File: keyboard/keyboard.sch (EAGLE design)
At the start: 39 parts, among them SW1 CHERRY_MX, SW10 CHERRY_MX, SW11 CHERRY_MX, SW12 CHERRY_MX, SW13 CHERRY_MX, SW14 CHERRY_MX, SW15 CHERRY_MX, SW16 CHERRY_MX, SW17 CHERRY_MX, SW18 CHERRY_MX, SW19 CHERRY_MX, SW2 CHERRY_MX, SW20 CHERRY_MX, SW21 CHERRY_MX, SW22 CHERRY_MX, SW23 CHERRY_MX, SW24 CHERRY_MX, SW25 CHERRY_MX, SW26 CHERRY_MX, SW27 CHERRY_MX, SW28 CHERRY_MX, SW3 CHERRY_MX, SW4 CHERRY_MX, SW5 CHERRY_MX, SW6 CHERRY_MX, SW7 CHERRY_MX, SW8 CHERRY_MX, SW9 CHERRY_MX

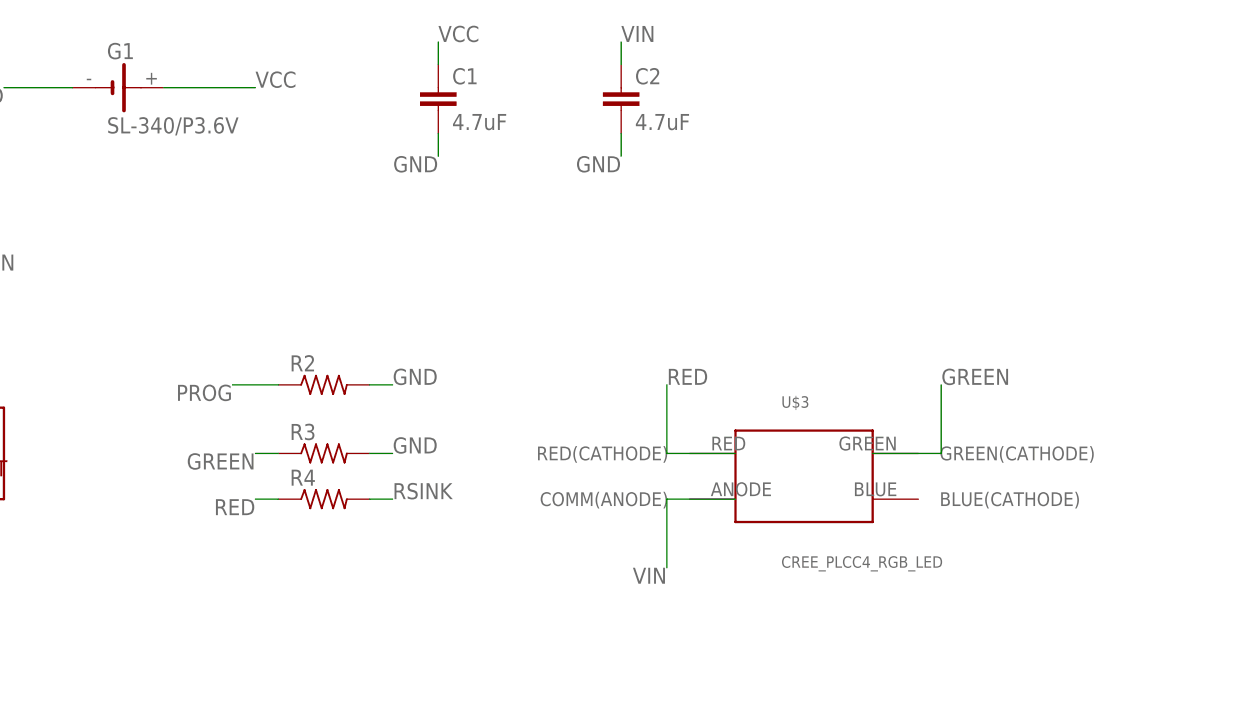
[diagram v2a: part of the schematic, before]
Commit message: add GRM32ER71H475KA88L capacitor
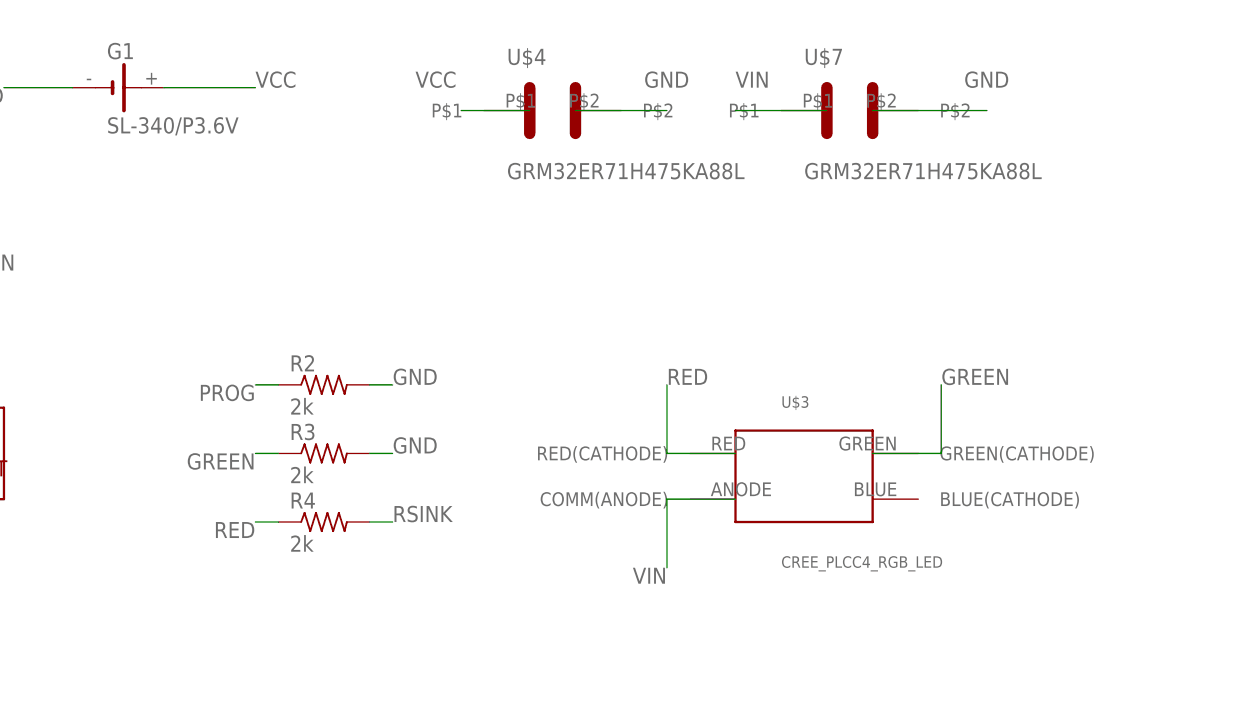
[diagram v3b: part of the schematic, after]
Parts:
- removed C1, C2: 4.7uF, capacitor-wima:C2.5/5
- added U$4, U$7: GRM32ER71H475KA88L, GRM32ER71H475KA88L:GRM32ER71H475KA88L
- R2, R3, R4: value (none) -> 2k
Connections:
- net GND: now also U$4.P$2, U$7.P$2; no longer C1.2, C2.2
- net VCC: now also U$4.P$1; no longer C1.1
- net VIN: now also U$7.P$1; no longer C2.1
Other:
- moved on the sheet: R4
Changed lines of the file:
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@@
 <part name="U$2" library="mcp73831t" deviceset="MCP73831T" device=""/>
 <part name="G1" library="battery" library_urn="urn:adsk.eagle:library:109" deviceset="SL-340/P3.6V" device="" package3d_urn="urn:adsk.eagle:package:4605/1"/>
-<part name="C1" library="capacitor-wima" library_urn="urn:adsk.eagle:library:116" deviceset="C" device="2.5/5" package3d_urn="urn:adsk.eagle:package:5407/1" value="4.7uF"/>
-<part name="C2" library="capacitor-wima" library_urn="urn:adsk.eagle:library:116" deviceset="C" device="2.5/5" package3d_urn="urn:adsk.eagle:package:5407/1" value="4.7uF"/>
 <part name="U$6" library="core51822b" deviceset="CORE51822B" device=""/>
-<part name="R2" library="resistor" library_urn="urn:adsk.eagle:library:348" deviceset="R-US_" device="R1210" package3d_urn="urn:adsk.eagle:package:26063/1"/>
-<part name="R3" library="resistor" library_urn="urn:adsk.eagle:library:348" deviceset="R-US_" device="R1210" package3d_urn="urn:adsk.eagle:package:26063/1"/>
-<part name="R4" library="resistor" library_urn="urn:adsk.eagle:library:348" deviceset="R-US_" device="R1210" package3d_urn="urn:adsk.eagle:package:26063/1"/>
+<part name="R2" library="resistor" library_urn="urn:adsk.eagle:library:348" deviceset="R-US_" device="R1210" package3d_urn="urn:adsk.eagle:package:26063/1" value="2k"/>
+<part name="R3" library="resistor" library_urn="urn:adsk.eagle:library:348" deviceset="R-US_" device="R1210" package3d_urn="urn:adsk.eagle:package:26063/1" value="2k"/>
+<part name="R4" library="resistor" library_urn="urn:adsk.eagle:library:348" deviceset="R-US_" device="R1210" package3d_urn="urn:adsk.eagle:package:26063/1" value="2k"/>
+<part name="U$4" library="GRM32ER71H475KA88L" deviceset="GRM32ER71H475KA88L" device=""/>
+<part name="U$7" library="GRM32ER71H475KA88L" deviceset="GRM32ER71H475KA88L" device=""/>
 </parts>
 <sheets>
@@
 <instance part="U$2" gate="G$1" x="45.72" y="33.02"/>
 <instance part="G1" gate="G$1" x="66.04" y="73.66"/>
-<instance part="C1" gate="G$1" x="101.6" y="73.66"/>
-<instance part="C2" gate="G$1" x="121.92" y="73.66"/>
 <instance part="U$6" gate="G$1" x="256.54" y="-264.16"/>
 <instance part="R2" gate="G$1" x="88.9" y="40.64"/>
 <instance part="R3" gate="G$1" x="88.9" y="33.02"/>
-<instance part="R4" gate="G$1" x="88.9" y="27.94"/>
+<instance part="R4" gate="G$1" x="88.9" y="25.4"/>
+<instance part="U$4" gate="G$1" x="114.3" y="71.12"/>
+<instance part="U$7" gate="G$1" x="147.32" y="71.12"/>
 </instances>
 <busses>
@@
 </segment>
 <segment>
-<pinref part="C1" gate="G$1" pin="2"/>
-<wire x1="101.6" y1="68.58" x2="101.6" y2="66.04" width="0.1524" layer="91"/>
-<label x="101.6" y="66.04" size="1.778" layer="95" rot="R180"/>
-</segment>
-<segment>
-<pinref part="C2" gate="G$1" pin="2"/>
-<wire x1="121.92" y1="68.58" x2="121.92" y2="66.04" width="0.1524" layer="91"/>
-<label x="121.92" y="66.04" size="1.778" layer="95" rot="R180"/>
-</segment>
-<segment>
 <pinref part="U$6" gate="G$1" pin="GND0"/>
 <wire x1="236.22" y1="-248.92" x2="218.44" y2="-248.92" width="0.1524" layer="91"/>
@@
 <wire x1="93.98" y1="40.64" x2="96.52" y2="40.64" width="0.1524" layer="91"/>
 <label x="96.52" y="40.64" size="1.778" layer="95"/>
+</segment>
+<segment>
+<pinref part="U$4" gate="G$1" pin="P$2"/>
+<wire x1="116.84" y1="71.12" x2="127" y2="71.12" width="0.1524" layer="91"/>
+<label x="124.46" y="73.66" size="1.778" layer="95"/>
+</segment>
+<segment>
+<pinref part="U$7" gate="G$1" pin="P$2"/>
+<wire x1="149.86" y1="71.12" x2="162.56" y2="71.12" width="0.1524" layer="91"/>
+<label x="160.02" y="73.66" size="1.778" layer="95"/>
 </segment>
 </net>
@@
 </segment>
 <segment>
-<pinref part="C1" gate="G$1" pin="1"/>
-<wire x1="101.6" y1="76.2" x2="101.6" y2="78.74" width="0.1524" layer="91"/>
-<label x="101.6" y="78.74" size="1.778" layer="95"/>
-</segment>
-<segment>
 <pinref part="U$6" gate="G$1" pin="VCC"/>
 <wire x1="236.22" y1="-276.86" x2="218.44" y2="-276.86" width="0.1524" layer="91"/>
 <label x="208.28" y="-276.86" size="1.778" layer="95"/>
+</segment>
+<segment>
+<pinref part="U$4" gate="G$1" pin="P$1"/>
+<wire x1="111.76" y1="71.12" x2="104.14" y2="71.12" width="0.1524" layer="91"/>
+<label x="99.06" y="73.66" size="1.778" layer="95"/>
 </segment>
 </net>
@@
 <segment>
 <pinref part="R4" gate="G$1" pin="1"/>
-<wire x1="83.82" y1="27.94" x2="81.28" y2="27.94" width="0.1524" layer="91"/>
-<label x="81.28" y="27.94" size="1.778" layer="95" rot="R180"/>
+<wire x1="83.82" y1="25.4" x2="81.28" y2="25.4" width="0.1524" layer="91"/>
+<label x="81.28" y="25.4" size="1.778" layer="95" rot="R180"/>
 </segment>
 </net>
@@
 <segment>
 <pinref part="R4" gate="G$1" pin="2"/>
-<wire x1="93.98" y1="27.94" x2="96.52" y2="27.94" width="0.1524" layer="91"/>
-<label x="96.52" y="27.94" size="1.778" layer="95"/>
+<wire x1="93.98" y1="25.4" x2="96.52" y2="25.4" width="0.1524" layer="91"/>
+<label x="96.52" y="25.4" size="1.778" layer="95"/>
 </segment>
 </net>
@@
 </segment>
 <segment>
-<pinref part="C2" gate="G$1" pin="1"/>
-<wire x1="121.92" y1="76.2" x2="121.92" y2="78.74" width="0.1524" layer="91"/>
-<label x="121.92" y="78.74" size="1.778" layer="95"/>
-</segment>
-<segment>
 <pinref part="U$2" gate="G$1" pin="4-VDD"/>
 <wire x1="50.8" y1="38.1" x2="50.8" y2="53.34" width="0.1524" layer="91"/>
 <label x="50.8" y="53.34" size="1.778" layer="95"/>
 </segment>
+<segment>
+<pinref part="U$7" gate="G$1" pin="P$1"/>
+<wire x1="144.78" y1="71.12" x2="134.62" y2="71.12" width="0.1524" layer="91"/>
+<label x="134.62" y="73.66" size="1.778" layer="95"/>
+</segment>
 </net>
 <net name="PROG" class="0">
@@
 <segment>
 <pinref part="R2" gate="G$1" pin="1"/>
-<wire x1="83.82" y1="40.64" x2="78.74" y2="40.64" width="0.1524" layer="91"/>
-<label x="78.74" y="40.64" size="1.778" layer="95" rot="R180"/>
-</segment>
-</net>
+<wire x1="83.82" y1="40.64" x2="81.28" y2="40.64" width="0.1524" layer="91"/>
+<label x="81.28" y="40.64" size="1.778" layer="95" rot="R180"/>
+</segment>
+</net>

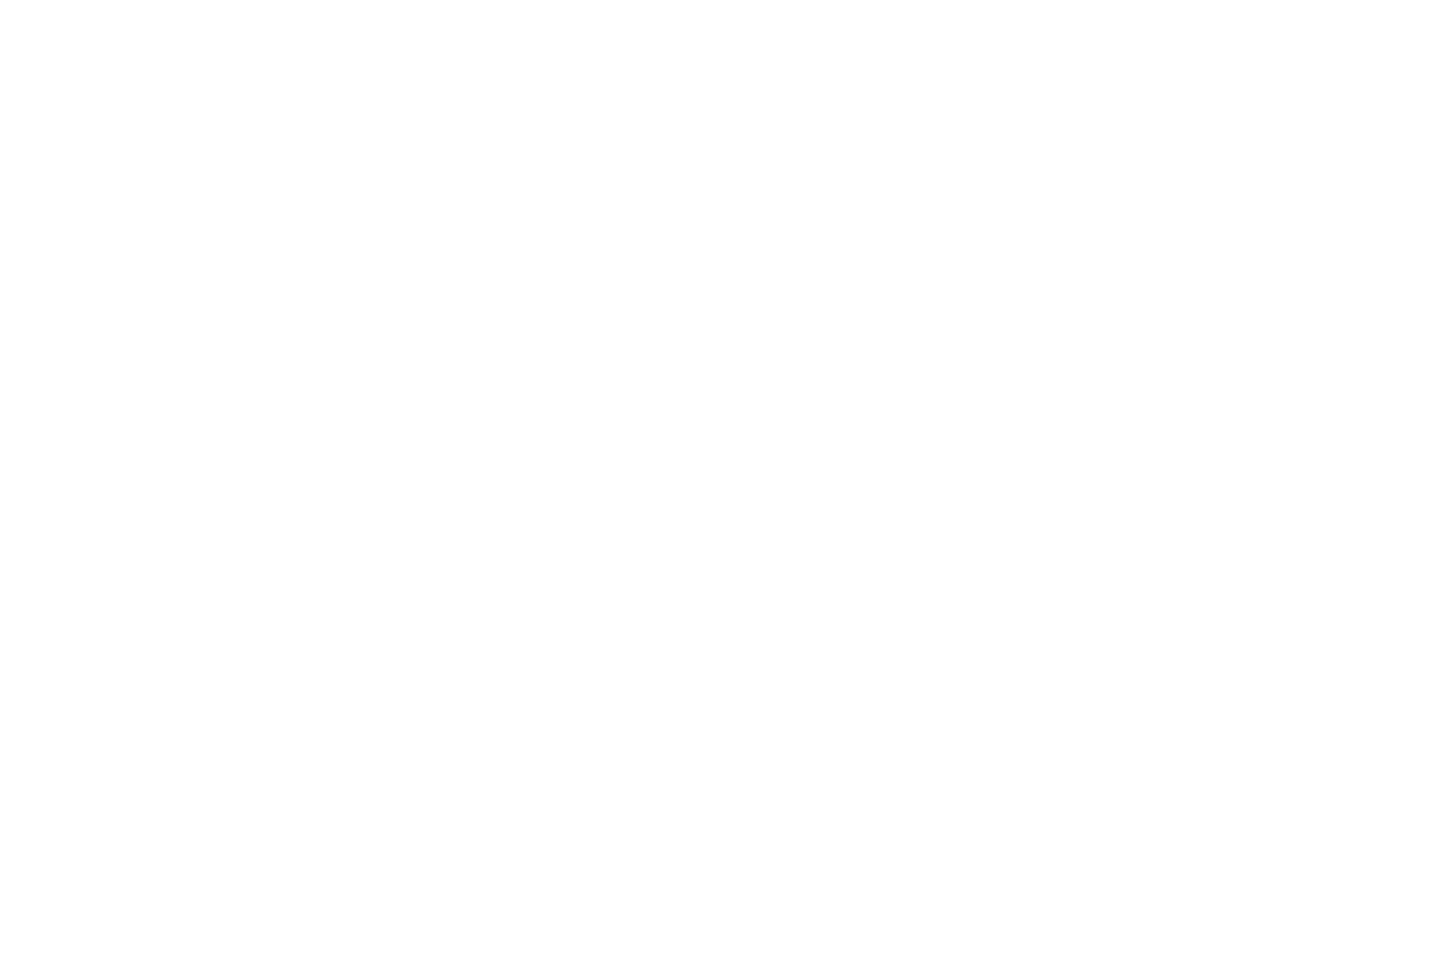
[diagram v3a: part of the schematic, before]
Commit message: mirror charging circuit on board bottom
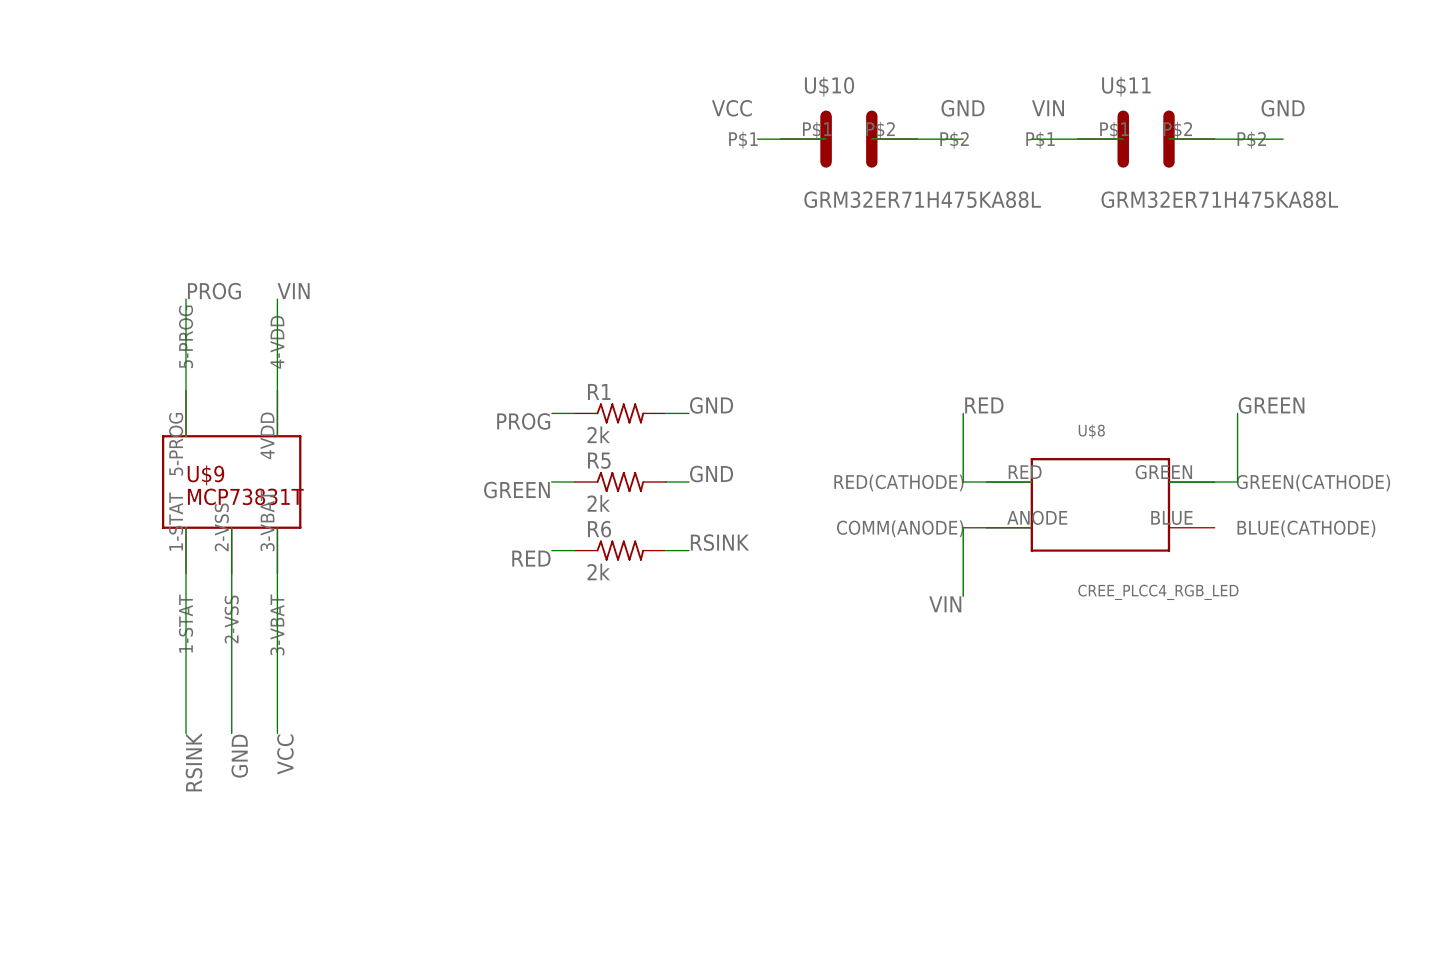
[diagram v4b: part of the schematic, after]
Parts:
- added R1, R5, R6: 2k, resistor:R-US_R1210
- added U$10, U$11: GRM32ER71H475KA88L, GRM32ER71H475KA88L:GRM32ER71H475KA88L
- added U$8: CREE_PLCC4_RGB_LED, cree_plcc4_rgb_led:CREE_PLCC4_RGB_LED
- added U$9: MCP73831T, mcp73831t:MCP73831T
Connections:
- net GND: now also R1.2, R5.2, U$10.P$2, U$11.P$2, U$9.2-VSS
- net GREEN: now also R5.1, U$8.GREEN(CATHODE)
- net PROG: now also R1.1, U$9.5-PROG
- net RED: now also R6.1, U$8.RED(CATHODE)
- net RSINK: now also R6.2, U$9.1-STAT
- net VCC: now also U$10.P$1, U$9.3-VBAT
- net VIN: now also U$11.P$1, U$8.COMM(ANODE), U$9.4-VDD
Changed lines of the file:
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@@
 <part name="U$4" library="GRM32ER71H475KA88L" deviceset="GRM32ER71H475KA88L" device=""/>
 <part name="U$7" library="GRM32ER71H475KA88L" deviceset="GRM32ER71H475KA88L" device=""/>
+<part name="U$8" library="cree_plcc4_rgb_led" deviceset="CREE_PLCC4_RGB_LED" device=""/>
+<part name="U$9" library="mcp73831t" deviceset="MCP73831T" device=""/>
+<part name="R1" library="resistor" library_urn="urn:adsk.eagle:library:348" deviceset="R-US_" device="R1210" package3d_urn="urn:adsk.eagle:package:26063/1" value="2k"/>
+<part name="R5" library="resistor" library_urn="urn:adsk.eagle:library:348" deviceset="R-US_" device="R1210" package3d_urn="urn:adsk.eagle:package:26063/1" value="2k"/>
+<part name="R6" library="resistor" library_urn="urn:adsk.eagle:library:348" deviceset="R-US_" device="R1210" package3d_urn="urn:adsk.eagle:package:26063/1" value="2k"/>
+<part name="U$10" library="GRM32ER71H475KA88L" deviceset="GRM32ER71H475KA88L" device=""/>
+<part name="U$11" library="GRM32ER71H475KA88L" deviceset="GRM32ER71H475KA88L" device=""/>
 </parts>
 <sheets>
@@
 <instance part="U$4" gate="G$1" x="114.3" y="71.12"/>
 <instance part="U$7" gate="G$1" x="147.32" y="71.12"/>
+<instance part="U$8" gate="G$1" x="365.76" y="25.4"/>
+<instance part="U$9" gate="G$1" x="269.24" y="27.94"/>
+<instance part="R1" gate="G$1" x="312.42" y="35.56"/>
+<instance part="R5" gate="G$1" x="312.42" y="27.94"/>
+<instance part="R6" gate="G$1" x="312.42" y="20.32"/>
+<instance part="U$10" gate="G$1" x="337.82" y="66.04"/>
+<instance part="U$11" gate="G$1" x="370.84" y="66.04"/>
 </instances>
 <busses>
@@
 <label x="160.02" y="73.66" size="1.778" layer="95"/>
 </segment>
+<segment>
+<pinref part="U$9" gate="G$1" pin="2-VSS"/>
+<wire x1="269.24" y1="22.86" x2="269.24" y2="0" width="0.1524" layer="91"/>
+<label x="269.24" y="0" size="1.778" layer="95" rot="R270"/>
+</segment>
+<segment>
+<pinref part="R5" gate="G$1" pin="2"/>
+<wire x1="317.5" y1="27.94" x2="320.04" y2="27.94" width="0.1524" layer="91"/>
+<label x="320.04" y="27.94" size="1.778" layer="95"/>
+</segment>
+<segment>
+<pinref part="R1" gate="G$1" pin="2"/>
+<wire x1="317.5" y1="35.56" x2="320.04" y2="35.56" width="0.1524" layer="91"/>
+<label x="320.04" y="35.56" size="1.778" layer="95"/>
+</segment>
+<segment>
+<pinref part="U$10" gate="G$1" pin="P$2"/>
+<wire x1="340.36" y1="66.04" x2="350.52" y2="66.04" width="0.1524" layer="91"/>
+<label x="347.98" y="68.58" size="1.778" layer="95"/>
+</segment>
+<segment>
+<pinref part="U$11" gate="G$1" pin="P$2"/>
+<wire x1="373.38" y1="66.04" x2="386.08" y2="66.04" width="0.1524" layer="91"/>
+<label x="383.54" y="68.58" size="1.778" layer="95"/>
+</segment>
 </net>
 <net name="SW1" class="0">
@@
 <label x="99.06" y="73.66" size="1.778" layer="95"/>
 </segment>
+<segment>
+<pinref part="U$9" gate="G$1" pin="3-VBAT"/>
+<wire x1="274.32" y1="22.86" x2="274.32" y2="0" width="0.1524" layer="91"/>
+<label x="274.32" y="0" size="1.778" layer="95" rot="R270"/>
+</segment>
+<segment>
+<pinref part="U$10" gate="G$1" pin="P$1"/>
+<wire x1="335.28" y1="66.04" x2="327.66" y2="66.04" width="0.1524" layer="91"/>
+<label x="322.58" y="68.58" size="1.778" layer="95"/>
+</segment>
 </net>
 <net name="RED" class="0">
@@
 <label x="81.28" y="25.4" size="1.778" layer="95" rot="R180"/>
 </segment>
+<segment>
+<pinref part="U$8" gate="G$1" pin="RED(CATHODE)"/>
+<wire x1="358.14" y1="27.94" x2="350.52" y2="27.94" width="0.1524" layer="91"/>
+<wire x1="350.52" y1="27.94" x2="350.52" y2="35.56" width="0.1524" layer="91"/>
+<label x="350.52" y="35.56" size="1.778" layer="95"/>
+</segment>
+<segment>
+<pinref part="R6" gate="G$1" pin="1"/>
+<wire x1="307.34" y1="20.32" x2="304.8" y2="20.32" width="0.1524" layer="91"/>
+<label x="304.8" y="20.32" size="1.778" layer="95" rot="R180"/>
+</segment>
 </net>
 <net name="GREEN" class="0">
@@
 <label x="81.28" y="33.02" size="1.778" layer="95" rot="R180"/>
 </segment>
+<segment>
+<pinref part="U$8" gate="G$1" pin="GREEN(CATHODE)"/>
+<wire x1="373.38" y1="27.94" x2="381" y2="27.94" width="0.1524" layer="91"/>
+<wire x1="381" y1="27.94" x2="381" y2="35.56" width="0.1524" layer="91"/>
+<label x="381" y="35.56" size="1.778" layer="95"/>
+</segment>
+<segment>
+<pinref part="R5" gate="G$1" pin="1"/>
+<wire x1="307.34" y1="27.94" x2="304.8" y2="27.94" width="0.1524" layer="91"/>
+<label x="304.8" y="27.94" size="1.778" layer="95" rot="R180"/>
+</segment>
 </net>
 <net name="RSINK" class="0">
@@
 <wire x1="93.98" y1="25.4" x2="96.52" y2="25.4" width="0.1524" layer="91"/>
 <label x="96.52" y="25.4" size="1.778" layer="95"/>
+</segment>
+<segment>
+<pinref part="U$9" gate="G$1" pin="1-STAT"/>
+<wire x1="264.16" y1="22.86" x2="264.16" y2="0" width="0.1524" layer="91"/>
+<label x="264.16" y="0" size="1.778" layer="95" rot="R270"/>
+</segment>
+<segment>
+<pinref part="R6" gate="G$1" pin="2"/>
+<wire x1="317.5" y1="20.32" x2="320.04" y2="20.32" width="0.1524" layer="91"/>
+<label x="320.04" y="20.32" size="1.778" layer="95"/>
 </segment>
 </net>
@@
 <label x="134.62" y="73.66" size="1.778" layer="95"/>
 </segment>
+<segment>
+<pinref part="U$8" gate="G$1" pin="COMM(ANODE)"/>
+<wire x1="358.14" y1="22.86" x2="350.52" y2="22.86" width="0.1524" layer="91"/>
+<wire x1="350.52" y1="22.86" x2="350.52" y2="15.24" width="0.1524" layer="91"/>
+<label x="350.52" y="15.24" size="1.778" layer="95" rot="R180"/>
+</segment>
+<segment>
+<pinref part="U$9" gate="G$1" pin="4-VDD"/>
+<wire x1="274.32" y1="33.02" x2="274.32" y2="48.26" width="0.1524" layer="91"/>
+<label x="274.32" y="48.26" size="1.778" layer="95"/>
+</segment>
+<segment>
+<pinref part="U$11" gate="G$1" pin="P$1"/>
+<wire x1="368.3" y1="66.04" x2="358.14" y2="66.04" width="0.1524" layer="91"/>
+<label x="358.14" y="68.58" size="1.778" layer="95"/>
+</segment>
 </net>
 <net name="PROG" class="0">
@@
 <label x="81.28" y="40.64" size="1.778" layer="95" rot="R180"/>
 </segment>
-</net>
+<segment>
+<pinref part="U$9" gate="G$1" pin="5-PROG"/>
+<wire x1="264.16" y1="33.02" x2="264.16" y2="48.26" width="0.1524" layer="91"/>
+<label x="264.16" y="48.26" size="1.778" layer="95"/>
+</segment>
+<segment>
+<pinref part="R1" gate="G$1" pin="1"/>
+<wire x1="307.34" y1="35.56" x2="304.8" y2="35.56" width="0.1524" layer="91"/>
+<label x="304.8" y="35.56" size="1.778" layer="95" rot="R180"/>
+</segment>
+</net>
